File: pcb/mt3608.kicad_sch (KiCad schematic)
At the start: 10 parts, among them U5 MT3608

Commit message: Split PCB into modules
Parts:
- renumbered C13 to C10, C14 to C11, C15 to C12, C16 to C13, D7 to D3, R23 to R10, R24 to R11, R22 to R9, U5 to U3
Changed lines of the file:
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@@
 		(dnp no)
 		(fields_autoplaced yes)
-		(property "Reference" "R23"
+		(property "Reference" "R10"
 			(at 86.36 49.5299 0)
 			(effects
@@
 		)
 		(instances
+			(project "ssd1322"
+				(path "/e965cf35-0f43-4e18-a922-fe79a625b049/f6fca6fe-a920-42ff-8a79-ce3664eefe2d"
+					(reference "R10")
+					(unit 1)
+				)
+			)
 			(project "bus_destination_sign"
 				(path "/ef60a031-d3da-483e-916d-caebb8513ab6/8bba229c-53cc-4db5-ae8c-5526ee00dbc6/66e7e007-2fa9-4a65-bc2c-9405a91bff95"
@@
 		(dnp no)
 		(fields_autoplaced yes)
-		(property "Reference" "C13"
+		(property "Reference" "C10"
 			(at 45.72 59.6899 0)
 			(effects
@@
 		)
 		(instances
+			(project "ssd1322"
+				(path "/e965cf35-0f43-4e18-a922-fe79a625b049/f6fca6fe-a920-42ff-8a79-ce3664eefe2d"
+					(reference "C10")
+					(unit 1)
+				)
+			)
 			(project "bus_destination_sign"
 				(path "/ef60a031-d3da-483e-916d-caebb8513ab6/8bba229c-53cc-4db5-ae8c-5526ee00dbc6/66e7e007-2fa9-4a65-bc2c-9405a91bff95"
@@
 		(dnp no)
 		(fields_autoplaced yes)
-		(property "Reference" "D7"
+		(property "Reference" "D3"
 			(at 79.0575 34.29 0)
 			(effects
@@
 		)
 		(instances
+			(project "ssd1322"
+				(path "/e965cf35-0f43-4e18-a922-fe79a625b049/f6fca6fe-a920-42ff-8a79-ce3664eefe2d"
+					(reference "D3")
+					(unit 1)
+				)
+			)
 			(project "bus_destination_sign"
 				(path "/ef60a031-d3da-483e-916d-caebb8513ab6/8bba229c-53cc-4db5-ae8c-5526ee00dbc6/66e7e007-2fa9-4a65-bc2c-9405a91bff95"
@@
 		(dnp no)
 		(fields_autoplaced yes)
-		(property "Reference" "#PWR014"
+		(property "Reference" "#PWR09"
 			(at 41.91 43.18 0)
 			(effects
@@
 		)
 		(instances
+			(project "ssd1322"
+				(path "/e965cf35-0f43-4e18-a922-fe79a625b049/f6fca6fe-a920-42ff-8a79-ce3664eefe2d"
+					(reference "#PWR09")
+					(unit 1)
+				)
+			)
 			(project "bus_destination_sign"
 				(path "/ef60a031-d3da-483e-916d-caebb8513ab6/8bba229c-53cc-4db5-ae8c-5526ee00dbc6/66e7e007-2fa9-4a65-bc2c-9405a91bff95"
@@
 		(dnp no)
 		(fields_autoplaced yes)
-		(property "Reference" "U5"
+		(property "Reference" "U3"
 			(at 64.77 43.18 0)
 			(effects
@@
 		)
 		(instances
+			(project "ssd1322"
+				(path "/e965cf35-0f43-4e18-a922-fe79a625b049/f6fca6fe-a920-42ff-8a79-ce3664eefe2d"
+					(reference "U3")
+					(unit 1)
+				)
+			)
 			(project "bus_destination_sign"
 				(path "/ef60a031-d3da-483e-916d-caebb8513ab6/8bba229c-53cc-4db5-ae8c-5526ee00dbc6/66e7e007-2fa9-4a65-bc2c-9405a91bff95"
@@
 		(dnp no)
 		(fields_autoplaced yes)
-		(property "Reference" "C16"
+		(property "Reference" "C13"
 			(at 135.89 59.6899 0)
 			(effects
@@
 		)
 		(instances
+			(project "ssd1322"
+				(path "/e965cf35-0f43-4e18-a922-fe79a625b049/f6fca6fe-a920-42ff-8a79-ce3664eefe2d"
+					(reference "C13")
+					(unit 1)
+				)
+			)
 			(project "bus_destination_sign"
 				(path "/ef60a031-d3da-483e-916d-caebb8513ab6/8bba229c-53cc-4db5-ae8c-5526ee00dbc6/66e7e007-2fa9-4a65-bc2c-9405a91bff95"
@@
 		(dnp no)
 		(fields_autoplaced yes)
-		(property "Reference" "#PWR015"
+		(property "Reference" "#PWR010"
 			(at 64.77 73.66 0)
 			(effects
@@
 		)
 		(instances
+			(project "ssd1322"
+				(path "/e965cf35-0f43-4e18-a922-fe79a625b049/f6fca6fe-a920-42ff-8a79-ce3664eefe2d"
+					(reference "#PWR010")
+					(unit 1)
+				)
+			)
 			(project "bus_destination_sign"
 				(path "/ef60a031-d3da-483e-916d-caebb8513ab6/8bba229c-53cc-4db5-ae8c-5526ee00dbc6/66e7e007-2fa9-4a65-bc2c-9405a91bff95"
@@
 		(dnp no)
 		(fields_autoplaced yes)
-		(property "Reference" "C15"
+		(property "Reference" "C12"
 			(at 118.11 59.6899 0)
 			(effects
@@
 		)
 		(instances
+			(project "ssd1322"
+				(path "/e965cf35-0f43-4e18-a922-fe79a625b049/f6fca6fe-a920-42ff-8a79-ce3664eefe2d"
+					(reference "C12")
+					(unit 1)
+				)
+			)
 			(project "bus_destination_sign"
 				(path "/ef60a031-d3da-483e-916d-caebb8513ab6/8bba229c-53cc-4db5-ae8c-5526ee00dbc6/66e7e007-2fa9-4a65-bc2c-9405a91bff95"
@@
 		(dnp no)
 		(fields_autoplaced yes)
-		(property "Reference" "R22"
+		(property "Reference" "R9"
 			(at 55.88 59.6899 0)
 			(effects
@@
 		)
 		(instances
+			(project "ssd1322"
+				(path "/e965cf35-0f43-4e18-a922-fe79a625b049/f6fca6fe-a920-42ff-8a79-ce3664eefe2d"
+					(reference "R9")
+					(unit 1)
+				)
+			)
 			(project "bus_destination_sign"
 				(path "/ef60a031-d3da-483e-916d-caebb8513ab6/8bba229c-53cc-4db5-ae8c-5526ee00dbc6/66e7e007-2fa9-4a65-bc2c-9405a91bff95"
@@
 		(dnp no)
 		(fields_autoplaced yes)
-		(property "Reference" "R24"
+		(property "Reference" "R11"
 			(at 86.36 59.6899 0)
 			(effects
@@
 		)
 		(instances
+			(project "ssd1322"
+				(path "/e965cf35-0f43-4e18-a922-fe79a625b049/f6fca6fe-a920-42ff-8a79-ce3664eefe2d"
+					(reference "R11")
+					(unit 1)
+				)
+			)
 			(project "bus_destination_sign"
 				(path "/ef60a031-d3da-483e-916d-caebb8513ab6/8bba229c-53cc-4db5-ae8c-5526ee00dbc6/66e7e007-2fa9-4a65-bc2c-9405a91bff95"
@@
 		(dnp no)
 		(fields_autoplaced yes)
-		(property "Reference" "C14"
+		(property "Reference" "C11"
 			(at 100.33 59.6899 0)
 			(effects
@@
 		)
 		(instances
+			(project "ssd1322"
+				(path "/e965cf35-0f43-4e18-a922-fe79a625b049/f6fca6fe-a920-42ff-8a79-ce3664eefe2d"
+					(reference "C11")
+					(unit 1)
+				)
+			)
 			(project "bus_destination_sign"
 				(path "/ef60a031-d3da-483e-916d-caebb8513ab6/8bba229c-53cc-4db5-ae8c-5526ee00dbc6/66e7e007-2fa9-4a65-bc2c-9405a91bff95"
@@
 		)
 		(instances
-			(project "bus_destination_sign"
-				(path "/ef60a031-d3da-483e-916d-caebb8513ab6/8bba229c-53cc-4db5-ae8c-5526ee00dbc6/66e7e007-2fa9-4a65-bc2c-9405a91bff95"
+			(project "ssd1322"
+				(path "/e965cf35-0f43-4e18-a922-fe79a625b049/f6fca6fe-a920-42ff-8a79-ce3664eefe2d"
+					(reference "L1")
+					(unit 1)
+				)
+			)
+			(project "bus_destination_sign"
+				(path "/ef60a031-d3da-483e-916d-caebb8513ab6/8bba229c-53cc-4db5-ae8c-5526ee00dbc6/66e7e007-2fa9-4a65-bc2c-9405a91bff95"

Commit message: SSD1327 PCB routing
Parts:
- renumbered C11 to C10, C12 to C11, C13 to C12, C10 to C9, D3 to D1, R11 to R10, R9 to R8, R10 to R9
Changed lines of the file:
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@@
 		(dnp no)
 		(fields_autoplaced yes)
-		(property "Reference" "R10"
+		(property "Reference" "R9"
 			(at 86.36 49.5299 0)
 			(effects
@@
 		)
 		(instances
+			(project "ssd1327"
+				(path "/4342a6a3-bef3-4d00-bf81-0e0627ac4f3c/66e7e007-2fa9-4a65-bc2c-9405a91bff95"
+					(reference "R9")
+					(unit 1)
+				)
+			)
 			(project "ssd1322"
 				(path "/e965cf35-0f43-4e18-a922-fe79a625b049/f6fca6fe-a920-42ff-8a79-ce3664eefe2d"
@@
 		(dnp no)
 		(fields_autoplaced yes)
-		(property "Reference" "C10"
+		(property "Reference" "C9"
 			(at 45.72 59.6899 0)
 			(effects
@@
 		)
 		(instances
+			(project "ssd1327"
+				(path "/4342a6a3-bef3-4d00-bf81-0e0627ac4f3c/66e7e007-2fa9-4a65-bc2c-9405a91bff95"
+					(reference "C9")
+					(unit 1)
+				)
+			)
 			(project "ssd1322"
 				(path "/e965cf35-0f43-4e18-a922-fe79a625b049/f6fca6fe-a920-42ff-8a79-ce3664eefe2d"
@@
 		(dnp no)
 		(fields_autoplaced yes)
-		(property "Reference" "D3"
+		(property "Reference" "D1"
 			(at 79.0575 34.29 0)
 			(effects
@@
 		)
 		(instances
+			(project "ssd1327"
+				(path "/4342a6a3-bef3-4d00-bf81-0e0627ac4f3c/66e7e007-2fa9-4a65-bc2c-9405a91bff95"
+					(reference "D1")
+					(unit 1)
+				)
+			)
 			(project "ssd1322"
 				(path "/e965cf35-0f43-4e18-a922-fe79a625b049/f6fca6fe-a920-42ff-8a79-ce3664eefe2d"
@@
 		)
 		(instances
+			(project "ssd1327"
+				(path "/4342a6a3-bef3-4d00-bf81-0e0627ac4f3c/66e7e007-2fa9-4a65-bc2c-9405a91bff95"
+					(reference "#PWR09")
+					(unit 1)
+				)
+			)
 			(project "ssd1322"
 				(path "/e965cf35-0f43-4e18-a922-fe79a625b049/f6fca6fe-a920-42ff-8a79-ce3664eefe2d"
@@
 		)
 		(instances
+			(project "ssd1327"
+				(path "/4342a6a3-bef3-4d00-bf81-0e0627ac4f3c/66e7e007-2fa9-4a65-bc2c-9405a91bff95"
+					(reference "U3")
+					(unit 1)
+				)
+			)
 			(project "ssd1322"
 				(path "/e965cf35-0f43-4e18-a922-fe79a625b049/f6fca6fe-a920-42ff-8a79-ce3664eefe2d"
@@
 		(dnp no)
 		(fields_autoplaced yes)
-		(property "Reference" "C13"
+		(property "Reference" "C12"
 			(at 135.89 59.6899 0)
 			(effects
@@
 		)
 		(instances
+			(project "ssd1327"
+				(path "/4342a6a3-bef3-4d00-bf81-0e0627ac4f3c/66e7e007-2fa9-4a65-bc2c-9405a91bff95"
+					(reference "C12")
+					(unit 1)
+				)
+			)
 			(project "ssd1322"
 				(path "/e965cf35-0f43-4e18-a922-fe79a625b049/f6fca6fe-a920-42ff-8a79-ce3664eefe2d"
@@
 		)
 		(instances
+			(project "ssd1327"
+				(path "/4342a6a3-bef3-4d00-bf81-0e0627ac4f3c/66e7e007-2fa9-4a65-bc2c-9405a91bff95"
+					(reference "#PWR010")
+					(unit 1)
+				)
+			)
 			(project "ssd1322"
 				(path "/e965cf35-0f43-4e18-a922-fe79a625b049/f6fca6fe-a920-42ff-8a79-ce3664eefe2d"
@@
 		(dnp no)
 		(fields_autoplaced yes)
-		(property "Reference" "C12"
+		(property "Reference" "C11"
 			(at 118.11 59.6899 0)
 			(effects
@@
 		)
 		(instances
+			(project "ssd1327"
+				(path "/4342a6a3-bef3-4d00-bf81-0e0627ac4f3c/66e7e007-2fa9-4a65-bc2c-9405a91bff95"
+					(reference "C11")
+					(unit 1)
+				)
+			)
 			(project "ssd1322"
 				(path "/e965cf35-0f43-4e18-a922-fe79a625b049/f6fca6fe-a920-42ff-8a79-ce3664eefe2d"
@@
 		(dnp no)
 		(fields_autoplaced yes)
-		(property "Reference" "R9"
+		(property "Reference" "R8"
 			(at 55.88 59.6899 0)
 			(effects
@@
 		)
 		(instances
+			(project "ssd1327"
+				(path "/4342a6a3-bef3-4d00-bf81-0e0627ac4f3c/66e7e007-2fa9-4a65-bc2c-9405a91bff95"
+					(reference "R8")
+					(unit 1)
+				)
+			)
 			(project "ssd1322"
 				(path "/e965cf35-0f43-4e18-a922-fe79a625b049/f6fca6fe-a920-42ff-8a79-ce3664eefe2d"
@@
 		(dnp no)
 		(fields_autoplaced yes)
-		(property "Reference" "R11"
+		(property "Reference" "R10"
 			(at 86.36 59.6899 0)
 			(effects
@@
 		)
 		(instances
+			(project "ssd1327"
+				(path "/4342a6a3-bef3-4d00-bf81-0e0627ac4f3c/66e7e007-2fa9-4a65-bc2c-9405a91bff95"
+					(reference "R10")
+					(unit 1)
+				)
+			)
 			(project "ssd1322"
 				(path "/e965cf35-0f43-4e18-a922-fe79a625b049/f6fca6fe-a920-42ff-8a79-ce3664eefe2d"
@@
 		(dnp no)
 		(fields_autoplaced yes)
-		(property "Reference" "C11"
+		(property "Reference" "C10"
 			(at 100.33 59.6899 0)
 			(effects
@@
 		)
 		(instances
+			(project "ssd1327"
+				(path "/4342a6a3-bef3-4d00-bf81-0e0627ac4f3c/66e7e007-2fa9-4a65-bc2c-9405a91bff95"
+					(reference "C10")
+					(unit 1)
+				)
+			)
 			(project "ssd1322"
 				(path "/e965cf35-0f43-4e18-a922-fe79a625b049/f6fca6fe-a920-42ff-8a79-ce3664eefe2d"
@@
 		)
 		(instances
-			(project "ssd1322"
-				(path "/e965cf35-0f43-4e18-a922-fe79a625b049/f6fca6fe-a920-42ff-8a79-ce3664eefe2d"
+			(project "ssd1327"
+				(path "/4342a6a3-bef3-4d00-bf81-0e0627ac4f3c/66e7e007-2fa9-4a65-bc2c-9405a91bff95"
+					(reference "L1")
+					(unit 1)
+				)
+			)
+			(project "ssd1322"
+				(path "/e965cf35-0f43-4e18-a922-fe79a625b049/f6fca6fe-a920-42ff-8a79-ce3664eefe2d"

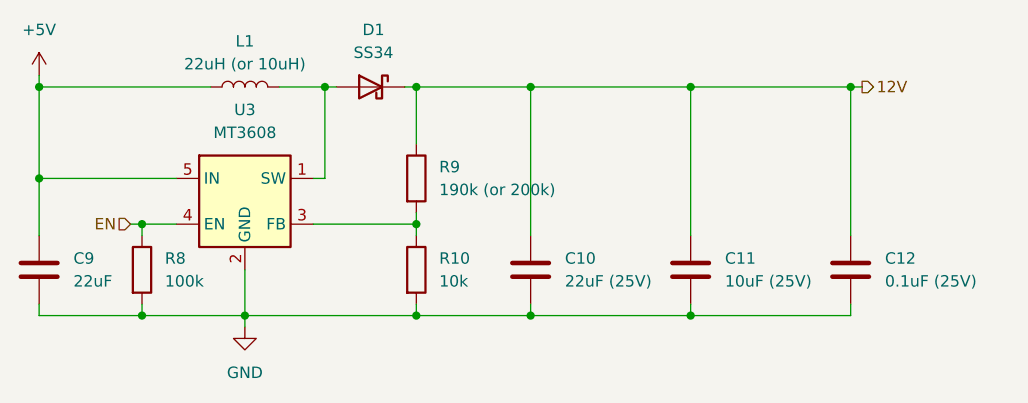
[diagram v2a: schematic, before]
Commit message: Master board PCB routing
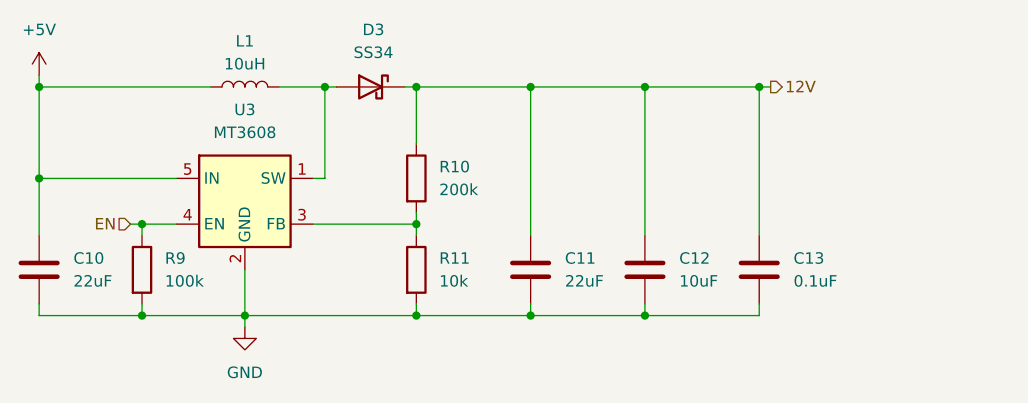
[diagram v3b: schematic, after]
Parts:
- C11: renamed from C10; value 22uF (25V) -> 22uF
- C12: renamed from C11; value 10uF (25V) -> 10uF
- C13: renamed from C12; value 0.1uF (25V) -> 0.1uF
- L1: value 22uH (or 10uH) -> 10uH
- R10: renamed from R9; value 190k (or 200k) -> 200k
- renumbered C9 to C10, D1 to D3, R10 to R11, R8 to R9
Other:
- moved on the sheet: C12, C13
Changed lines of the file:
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@@
-	)
-	(junction
-		(at 114.3 66.04)
-		(diameter 0)
-		(color 0 0 0 0)
 	)
 	(junction
@@
 	)
 	(junction
-		(at 132.08 40.64)
+		(at 121.92 40.64)
 		(diameter 0)
 		(color 0 0 0 0)
@@
 	)
 	(junction
-		(at 114.3 40.64)
+		(at 109.22 66.04)
 		(diameter 0)
 		(color 0 0 0 0)
@@
 		(color 0 0 0 0)
 	)
+	(junction
+		(at 109.22 40.64)
+		(diameter 0)
+		(color 0 0 0 0)
+	)
 	(wire
 		(pts
@@
 	(wire
 		(pts
-			(xy 114.3 66.04) (xy 96.52 66.04)
+			(xy 109.22 66.04) (xy 121.92 66.04)
 		)
 		(stroke
@@
 	(wire
 		(pts
-			(xy 132.08 40.64) (xy 133.35 40.64)
-		)
-		(stroke
-			(width 0)
-			(type default)
-		)
-	)
-	(wire
-		(pts
-			(xy 114.3 66.04) (xy 132.08 66.04)
-		)
-		(stroke
-			(width 0)
-			(type default)
-		)
-	)
-	(wire
-		(pts
 			(xy 41.91 50.8) (xy 41.91 57.15)
 		)
@@
 	(wire
 		(pts
-			(xy 132.08 64.77) (xy 132.08 66.04)
+			(xy 121.92 64.77) (xy 121.92 66.04)
 		)
 		(stroke
@@
 	(wire
 		(pts
+			(xy 109.22 66.04) (xy 96.52 66.04)
+		)
+		(stroke
+			(width 0)
+			(type default)
+		)
+	)
+	(wire
+		(pts
 			(xy 53.34 64.77) (xy 53.34 66.04)
 		)
@@
 	(wire
 		(pts
-			(xy 132.08 40.64) (xy 132.08 57.15)
+			(xy 121.92 40.64) (xy 121.92 57.15)
 		)
 		(stroke
@@
 	(wire
 		(pts
-			(xy 114.3 40.64) (xy 114.3 57.15)
+			(xy 109.22 40.64) (xy 109.22 57.15)
 		)
 		(stroke
@@
 	(wire
 		(pts
-			(xy 114.3 40.64) (xy 132.08 40.64)
-		)
-		(stroke
-			(width 0)
-			(type default)
-		)
-	)
-	(wire
-		(pts
 			(xy 53.34 66.04) (xy 64.77 66.04)
 		)
@@
 	(wire
 		(pts
+			(xy 109.22 40.64) (xy 121.92 40.64)
+		)
+		(stroke
+			(width 0)
+			(type default)
+		)
+	)
+	(wire
+		(pts
 			(xy 64.77 66.04) (xy 64.77 60.96)
 		)
@@
 	(wire
 		(pts
-			(xy 96.52 40.64) (xy 114.3 40.64)
+			(xy 96.52 40.64) (xy 109.22 40.64)
 		)
 		(stroke
@@
 	(wire
 		(pts
-			(xy 114.3 64.77) (xy 114.3 66.04)
+			(xy 109.22 64.77) (xy 109.22 66.04)
+		)
+		(stroke
+			(width 0)
+			(type default)
+		)
+	)
+	(wire
+		(pts
+			(xy 121.92 40.64) (xy 123.19 40.64)
 		)
 		(stroke
@@
 	(hierarchical_label "12V"
 		(shape output)
-		(at 133.35 40.64 0)
+		(at 123.19 40.64 0)
 		(effects
 			(font
@@
 		(dnp no)
 		(fields_autoplaced yes)
-		(property "Reference" "R9"
+		(property "Reference" "R10"
 			(at 86.36 49.5299 0)
 			(effects
@@
 			)
 		)
-		(property "Value" "190k (or 200k)"
+		(property "Value" "200k"
 			(at 86.36 52.0699 0)
 			(effects
@@
 		(dnp no)
 		(fields_autoplaced yes)
-		(property "Reference" "C9"
+		(property "Reference" "C10"
 			(at 45.72 59.6899 0)
 			(effects
@@
 		(dnp no)
 		(fields_autoplaced yes)
-		(property "Reference" "D1"
+		(property "Reference" "D3"
 			(at 79.0575 34.29 0)
 			(effects
@@
 	(symbol
 		(lib_id "Device:C")
-		(at 132.08 60.96 0)
+		(at 121.92 60.96 0)
 		(unit 1)
 		(exclude_from_sim no)
@@
 		(dnp no)
 		(fields_autoplaced yes)
-		(property "Reference" "C12"
-			(at 135.89 59.6899 0)
-			(effects
-				(font
-					(size 1.27 1.27)
-				)
-				(justify left)
-			)
-		)
-		(property "Value" "0.1uF (25V)"
-			(at 135.89 62.2299 0)
+		(property "Reference" "C13"
+			(at 125.73 59.6899 0)
+			(effects
+				(font
+					(size 1.27 1.27)
+				)
+				(justify left)
+			)
+		)
+		(property "Value" "0.1uF"
+			(at 125.73 62.2299 0)
 			(effects
 				(font
@@
 		)
 		(property "Footprint" "Capacitor_SMD:C_0603_1608Metric"
-			(at 133.0452 64.77 0)
+			(at 122.8852 64.77 0)
 			(effects
 				(font
@@
 		)
 		(property "Datasheet" "~"
-			(at 132.08 60.96 0)
+			(at 121.92 60.96 0)
 			(effects
 				(font
@@
 		)
 		(property "Description" "Unpolarized capacitor"
-			(at 132.08 60.96 0)
+			(at 121.92 60.96 0)
 			(effects
 				(font
@@
 	(symbol
 		(lib_id "Device:C")
-		(at 114.3 60.96 0)
+		(at 109.22 60.96 0)
 		(unit 1)
 		(exclude_from_sim no)
@@
 		(dnp no)
 		(fields_autoplaced yes)
-		(property "Reference" "C11"
-			(at 118.11 59.6899 0)
-			(effects
-				(font
-					(size 1.27 1.27)
-				)
-				(justify left)
-			)
-		)
-		(property "Value" "10uF (25V)"
-			(at 118.11 62.2299 0)
+		(property "Reference" "C12"
+			(at 113.03 59.6899 0)
+			(effects
+				(font
+					(size 1.27 1.27)
+				)
+				(justify left)
+			)
+		)
+		(property "Value" "10uF"
+			(at 113.03 62.2299 0)
 			(effects
 				(font
@@
 		)
 		(property "Footprint" "Capacitor_SMD:C_0603_1608Metric"
-			(at 115.2652 64.77 0)
+			(at 110.1852 64.77 0)
 			(effects
 				(font
@@
 		)
 		(property "Datasheet" "~"
-			(at 114.3 60.96 0)
+			(at 109.22 60.96 0)
 			(effects
 				(font
@@
 		)
 		(property "Description" "Unpolarized capacitor"
-			(at 114.3 60.96 0)
+			(at 109.22 60.96 0)
 			(effects
 				(font
@@
 		(dnp no)
 		(fields_autoplaced yes)
-		(property "Reference" "R8"
+		(property "Reference" "R9"
 			(at 55.88 59.6899 0)
 			(effects
@@
 		(dnp no)
 		(fields_autoplaced yes)
-		(property "Reference" "R10"
+		(property "Reference" "R11"
 			(at 86.36 59.6899 0)
 			(effects
@@
 		(dnp no)
 		(fields_autoplaced yes)
-		(property "Reference" "C10"
+		(property "Reference" "C11"
 			(at 100.33 59.6899 0)
 			(effects
@@
 			)
 		)
-		(property "Value" "22uF (25V)"
+		(property "Value" "22uF"
 			(at 100.33 62.2299 0)
 			(effects
@@
 			)
 		)
-		(property "Value" "22uH (or 10uH)"
+		(property "Value" "10uH"
 			(at 64.77 38.1 90)
 			(effects
